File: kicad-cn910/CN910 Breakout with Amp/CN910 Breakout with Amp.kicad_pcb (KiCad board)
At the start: 2 copper layers, 46 x 32 mm, 35 parts, among them J1 CN910_FPC_CON, J2 PB_RF_OUT, J3 USB4125-GF-A-0190_REVA2, SW1 SW_SPDT, U1 ADA4857, U2 AP7375-50SR-7

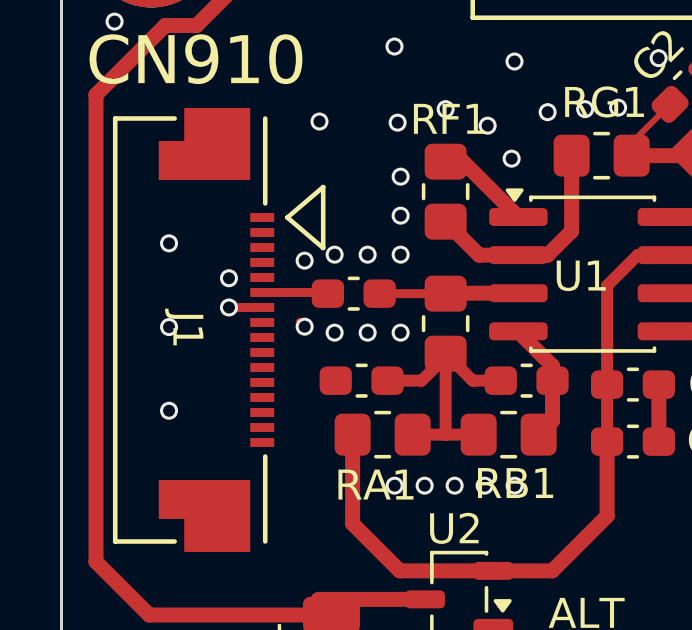
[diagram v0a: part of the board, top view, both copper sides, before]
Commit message: Fixed CN910 pin 7/8 routing in the breakout with amp design. RF_AGC_IN (pin 7) was mistakenly tied to GND instead of REG_GND (pin 8).
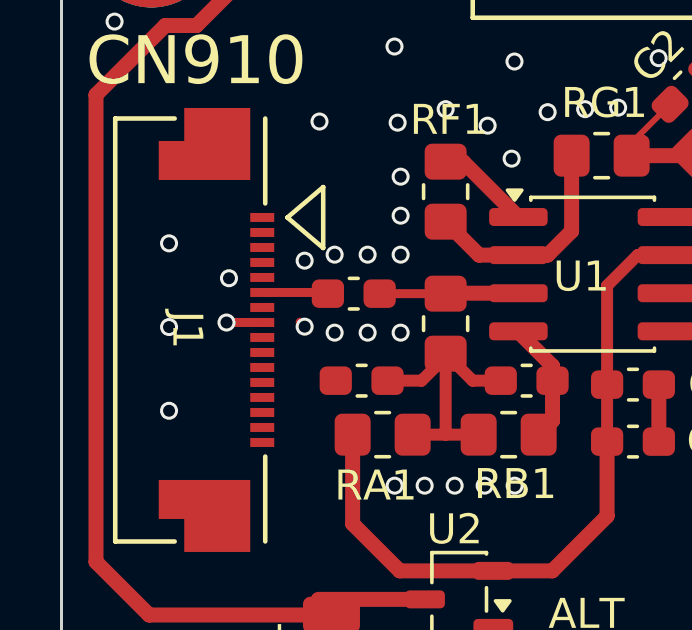
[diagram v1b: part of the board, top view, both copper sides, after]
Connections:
- J1 pad 7: GND -> unconnected-(J1-RF_AGC_IN-Pad7)
- J1 pad 8: unconnected-(J1-REG_GND-Pad8) -> GND
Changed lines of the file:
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@@
 		(sheetname "/")
 		(sheetfile "CN910 Breakout with Amp.kicad_sch")
+		(units
+			(unit
+				(name "A")
+				(pins "P1" "P2" "1" "2" "3" "4" "5" "6" "7" "8" "9" "10" "11" "12" "13"
+					"14" "15" "16"
+				)
+			)
+		)
 		(clearance 0.1)
 		(attr smd)
@@
 			(size 0.3 0.8)
 			(layers "F.Cu" "F.Mask" "F.Paste")
-			(net "GND")
+			(net "unconnected-(J1-RF_AGC_IN-Pad7)")
 			(pinfunction "RF_AGC_IN_7")
-			(pintype "input")
+			(pintype "input+no_connect")
 			(zone_connect 1)
 		)
@@
 			(size 0.3 0.8)
 			(layers "F.Cu" "F.Mask" "F.Paste")
-			(net "unconnected-(J1-REG_GND-Pad8)")
+			(net "GND")
 			(pinfunction "REG_GND_8")
-			(pintype "passive+no_connect")
+			(pintype "passive")
 			(clearance 0.1)
 		)
@@
 		(sheetname "/")
 		(sheetfile "CN910 Breakout with Amp.kicad_sch")
+		(units
+			(unit
+				(name "A")
+				(pins "1" "2")
+			)
+		)
 		(attr through_hole)
 		(duplicate_pad_numbers_are_jumpers no)
@@
 		(sheetname "/Amplifier/")
 		(sheetfile "amp.kicad_sch")
+		(units
+			(unit
+				(name "A")
+				(pins "2" "1" "3")
+			)
+		)
 		(attr through_hole)
 		(duplicate_pad_numbers_are_jumpers no)
@@
 	)
 	(segment
-		(start 116.367254 118.975374)
-		(end 115.904753 119.437875)
-		(width 0.5)
+		(start 105.501678 115.698322)
+		(end 105.5 115.7)
+		(width 0.3)
 		(layer "F.Cu")
 		(net "GND")
 	)
 	(segment
-		(start 105.582296 115.198321)
-		(end 106.691428 115.198321)
-		(width 0.3)
+		(start 116.367254 118.975374)
+		(end 115.904753 119.437875)
+		(width 0.5)
 		(layer "F.Cu")
 		(net "GND")
@@
 		(net "GND")
 	)
+	(segment
+		(start 106.691428 115.698322)
+		(end 105.501678 115.698322)
+		(width 0.3)
+		(layer "F.Cu")
+		(net "GND")
+	)
 	(via
 		(at 115.004753 110.237874)
@@
 	)
 	(via
-		(at 105.582296 115.198321)
-		(size 0.6)
-		(drill 0.4)
-		(layers "F.Cu" "B.Cu")
-		(free yes)
-		(net "GND")
-	)
-	(via
 		(at 118.554753 108.537874)
 		(size 0.6)
@@
 		(size 0.6)
 		(drill 0.4)
+		(layers "F.Cu" "B.Cu")
+		(free yes)
+		(net "GND")
+	)
+	(via
+		(at 105.5 115.7)
+		(size 0.6)
+		(drill 0.4)
